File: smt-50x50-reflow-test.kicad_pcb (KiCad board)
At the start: 4 copper layers, 50 x 50 mm, 113 parts, among them J1 Conn_01x04_Pin, J2 Conn_01x02, J3 Conn_01x01, J4 USB_C_Receptacle_USB2.0_14P, J5 Conn_01x01, J6 Conn_01x01, J7 Conn_01x01, J8 Conn_01x04_Pin, J9 Conn_01x03_Pin, SW1 SW_Push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

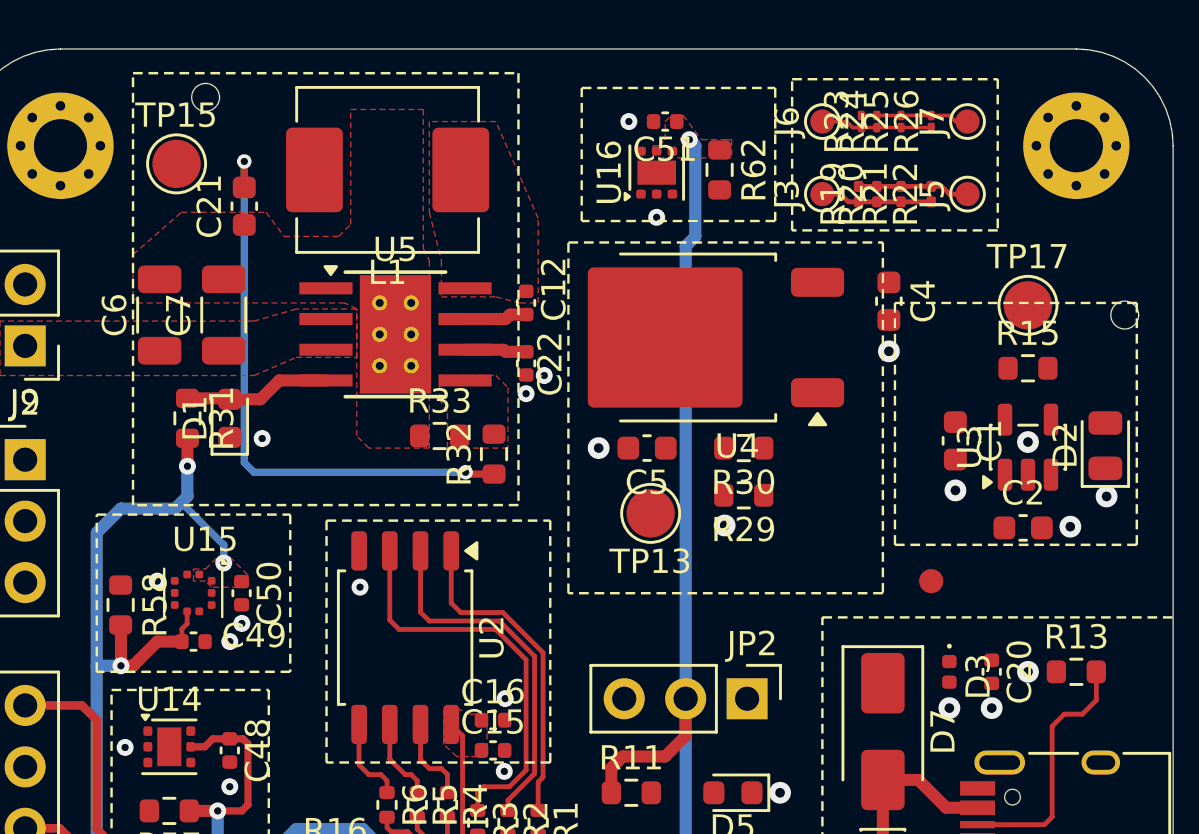
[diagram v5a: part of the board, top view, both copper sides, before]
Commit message: pcb: add 5v routing
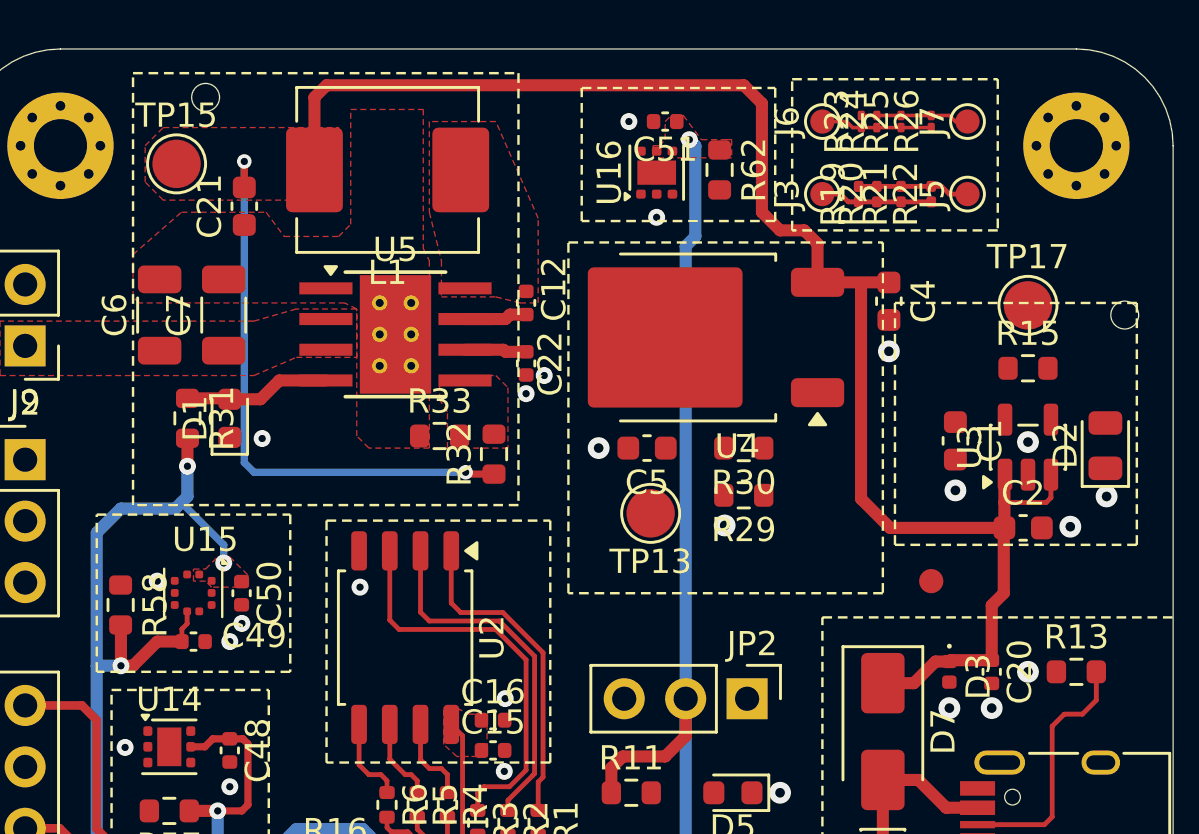
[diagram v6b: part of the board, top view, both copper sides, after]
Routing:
- net +5V: track 24.0 -> 88.8 mm
- added copper zone on F.Cu, net +5V

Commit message: pcb: add power section routing
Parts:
- moved TP13 1.17 mm to (162.2, 94.0)
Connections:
- C1 pad 1: Net-(U3-VOUT) -> Net-(JP2-A)
- JP2 pad 1: Net-(D2-A) -> Net-(JP2-A)
- R15 pad 1: Net-(U3-VOUT) -> Net-(JP2-A)
- TP17 pad 1: Net-(U3-VOUT) -> Net-(JP2-A)
- U3 pad 5: Net-(U3-VOUT) -> Net-(JP2-A)
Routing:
- net Net-(JP2-B): track 0.00 -> 19.0 mm
- net Net-(JP2-A): track 0.00 -> 18.6 mm, vias 0 -> 1
- net Net-(U4-ADJ): track 0.00 -> 6.20 mm
- net Net-(D2-A): track 0.00 -> 4.49 mm
- added copper zone on F.Cu, net Net-(JP2-A)

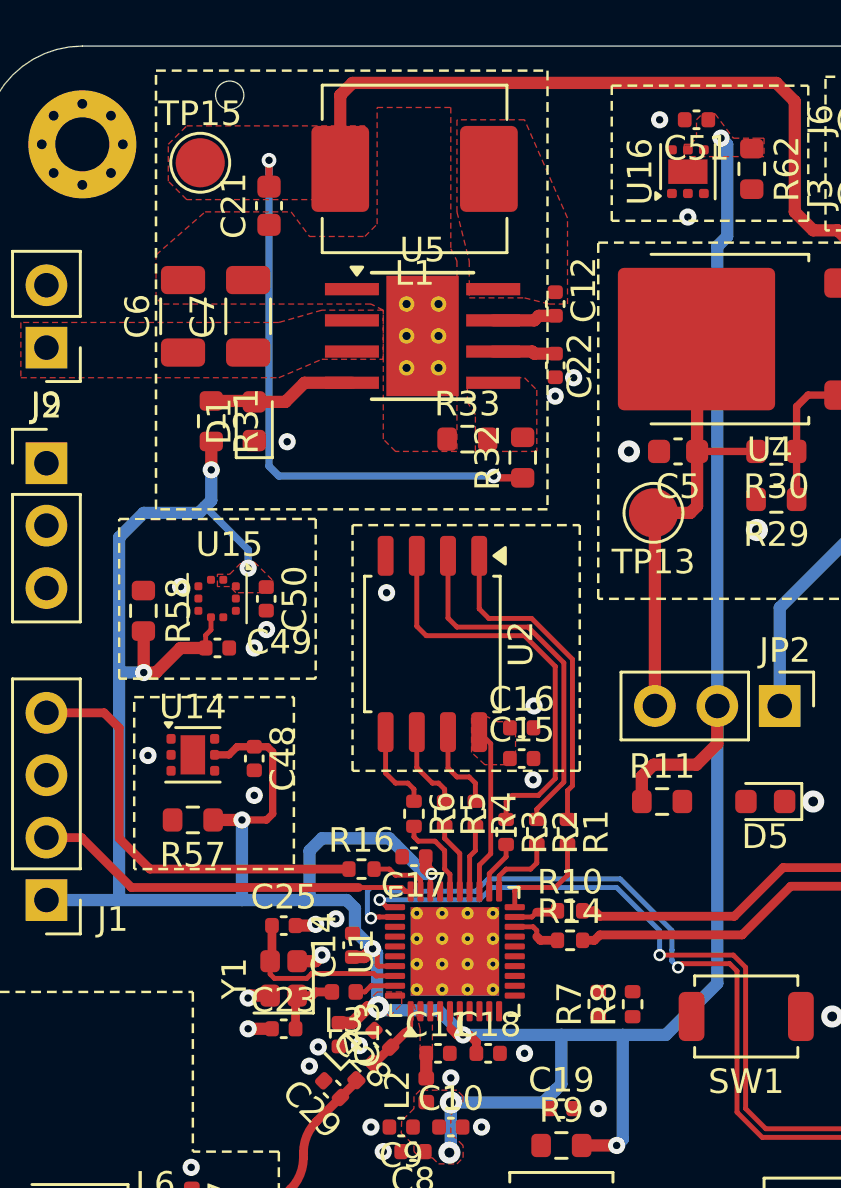
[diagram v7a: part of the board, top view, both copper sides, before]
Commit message: pcb: add i2c routing
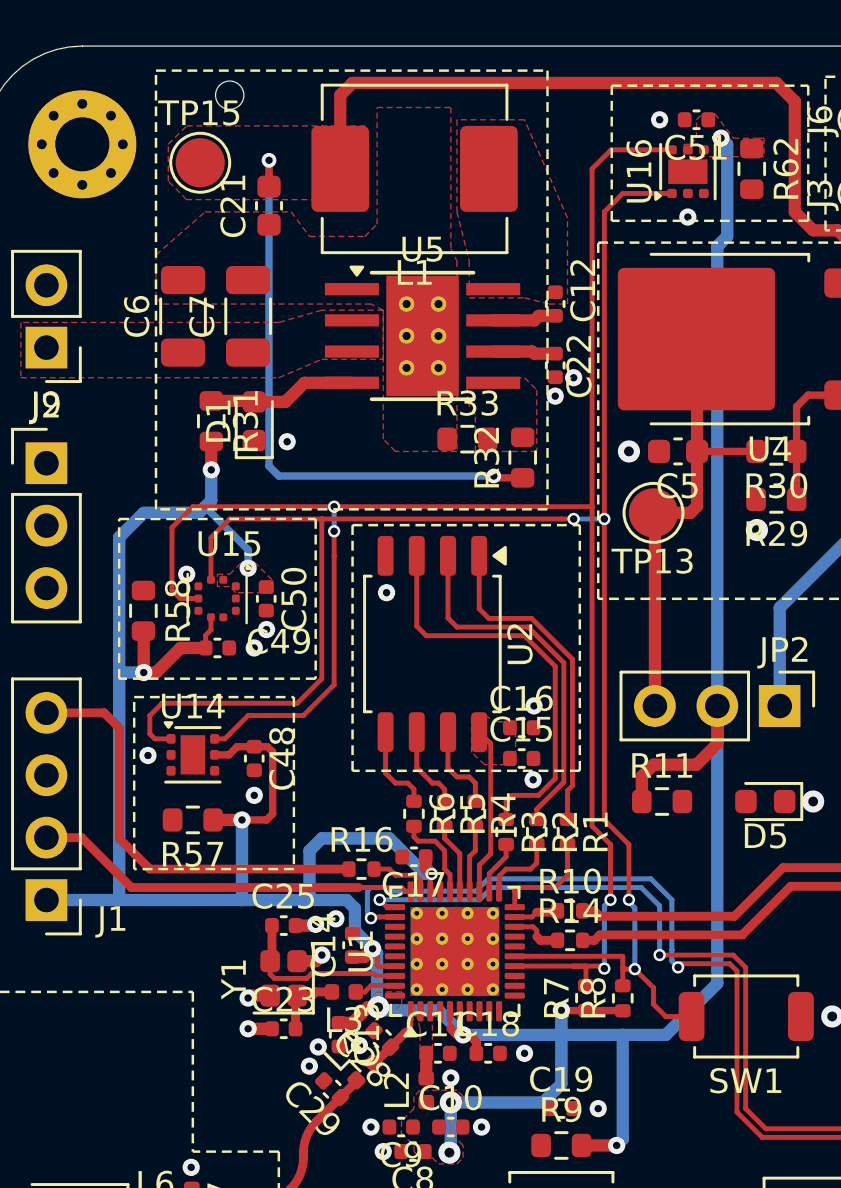
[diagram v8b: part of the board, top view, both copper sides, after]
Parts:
- moved R7 0.55 mm to (159.5, 113.8)
- moved R8 0.47 mm to (161.0, 113.8)
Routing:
- net /BOOT/SCL: track 0.00 -> 77.9 mm, vias 0 -> 4
- net /SDA: track 0.00 -> 75.8 mm, vias 0 -> 4
- net +3V3: track 146.7 -> 150.2 mm, vias 12 -> 13
- net Net-(U1-GPIO19/SDIO_CLK/FSPICS3): track 34.3 -> 35.0 mm
- net Net-(U1-GPIO18/SDIO_CMD/FSPICS2): track 29.5 -> 30.1 mm
